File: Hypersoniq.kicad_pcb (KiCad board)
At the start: 4 copper layers, 40.4 x 100 mm, 133 parts, among them J1 Conn_01x10_Pin, J2 Conn_01x10_Pin, J3 Conn_01x10_Pin, J4 Eurorack_10_pin_power, U1 TL074, U2 SSI2140, U3 SSI2140, U4 SSI2140, U5 SSI2140, U6 TL072

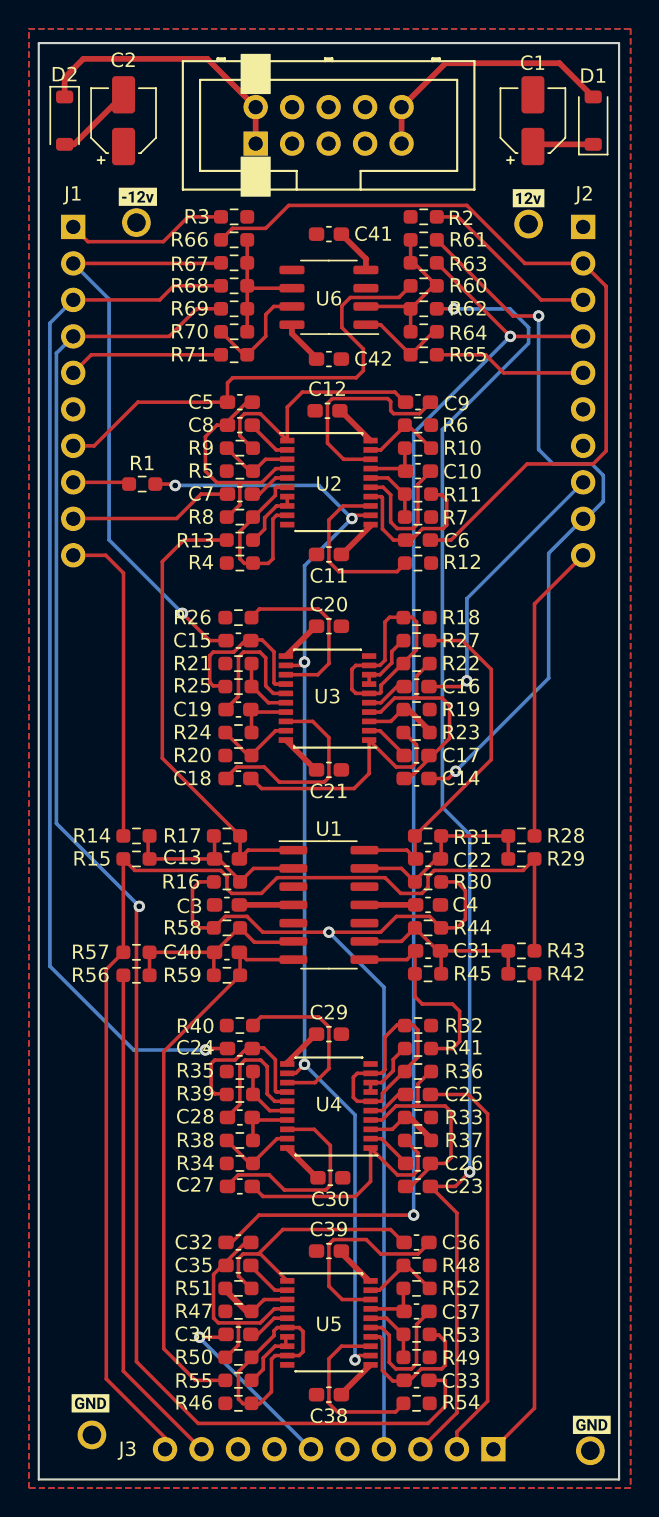
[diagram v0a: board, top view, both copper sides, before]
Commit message: First draft of PCB layout complete
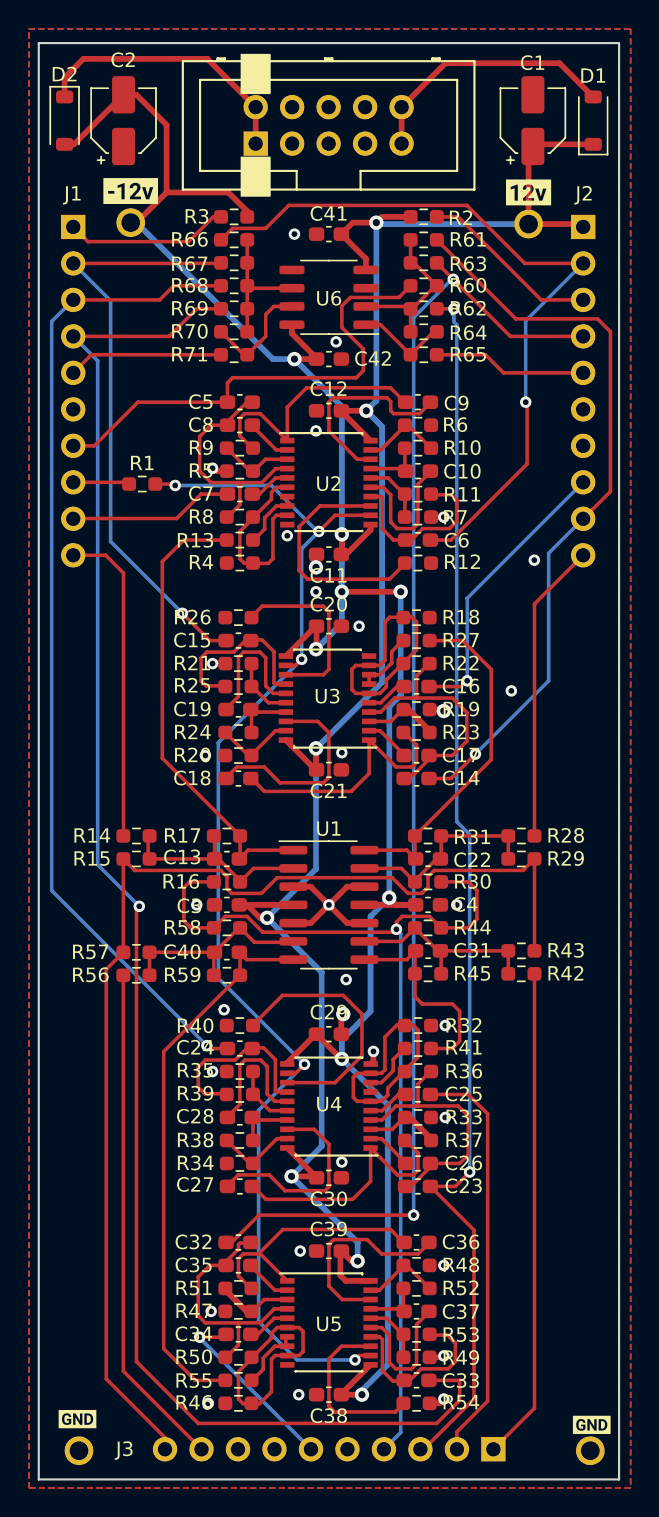
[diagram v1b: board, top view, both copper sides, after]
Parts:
- removed kibuzzard-640237A8: G***, kibuzzard-640237A8
- removed kibuzzard-640237FD: G***, kibuzzard-640237FD
- added kibuzzard-64BBE4CA: G***, kibuzzard-64BBE4CA, F.Cu at (56.4, 60.3)
- added kibuzzard-64BBE4D7: G***, kibuzzard-64BBE4D7, F.Cu at (84.1, 60.4)
- moved kibuzzard-640237DF 1.42 mm to (52.7, 145.8)
- moved TP4 1.42 mm to (52.8, 148.0)
- moved TP2 0.40 mm to (56.4, 62.5)
- moved C12 0.10 mm to (70.2, 75.6)
- moved C30 0.10 mm to (70.2, 129.0)
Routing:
- net -12V: track 24.1 -> 154.3 mm, vias 0 -> 8
- net +12V: track 23.3 -> 139.2 mm, vias 0 -> 6
- net GND: track 0.00 -> 21.3 mm, vias 0 -> 33
- net /Q_CONTROL: track 81.5 -> 90.3 mm
- net /1POLE_OUT3: track 92.3 -> 86.1 mm
- net Net-(U4-Q_VCA_IN+): track 12.0 -> 17.9 mm
- net Net-(U2-Q_VCA_IN+): track 12.0 -> 16.7 mm
- net /4POLE_OUT1: track 56.4 -> 52.5 mm, vias 0 -> 1
- net /4POLE_OUT3: track 72.6 -> 69.2 mm
- net /1POLE_OUT4: track 90.1 -> 92.5 mm
- net Net-(U3-OUT1): track 15.6 -> 18.0 mm
- net /FREQ_POT: track 66.4 -> 68.8 mm
- net Net-(U5-OUT1): track 14.9 -> 17.2 mm
- net Net-(U4-OUT1): track 16.5 -> 18.6 mm
- net Net-(U4-OUT4): track 11.3 -> 12.9 mm
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- removed copper zone on In1.Cu, net GND
- removed copper zone on In2.Cu, net GND
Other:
- copper layers 4 -> 2

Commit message: Controls PCB lay out
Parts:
- added kibuzzard-64BBF567: G***, kibuzzard-64BBF567, F.Cu at (83.9, 143.8)
- added kibuzzard-64BBF56E: G***, kibuzzard-64BBF56E, F.Cu at (83.8, 129.0)
- added kibuzzard-64BBF574: G***, kibuzzard-64BBF574, F.Cu at (84.1, 100.4)
- added kibuzzard-64BBF597: G***, kibuzzard-64BBF597, F.Cu at (83.8, 85.3)
- added kibuzzard-64BBF5E4: G***, kibuzzard-64BBF5E4, F.Cu at (83.0, 68.0)
- added kibuzzard-64BBF60A: G***, kibuzzard-64BBF60A, F.Cu at (87.4, 110.0)
- moved kibuzzard-64BBE4CA 0.32 mm to (56.5, 60.0)
- moved kibuzzard-640237DF 0.32 mm to (88.4, 145.9)
- moved kibuzzard-64BBE4D7 0.20 mm to (84.1, 60.2)
- moved TP4 0.16 mm to (52.6, 148.1)
- moved R1 0.10 mm to (57.2, 80.6)
- moved kibuzzard-640237DF 0.10 mm to (52.6, 145.8)
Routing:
- net /Filter_Voice4/FREQ_CONTROL: track 39.0 -> 37.7 mm
- net Net-(U2-OUT2): track 18.3 -> 17.2 mm
- net /4POLE_OUT3: track 69.2 -> 70.2 mm
- net Net-(U4-Q_VCA_IN+): track 17.9 -> 18.8 mm
- net Net-(U4-OUT2): track 18.2 -> 17.3 mm
- net /1POLE_OUT4: track 92.5 -> 93.2 mm
- net GND: vias 33 -> 73
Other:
- board text added: "Hypersoniq v1.0 2023 Mountjoy Modular SSI2140 HP Filter"
